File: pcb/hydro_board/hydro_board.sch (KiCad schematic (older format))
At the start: 1 part

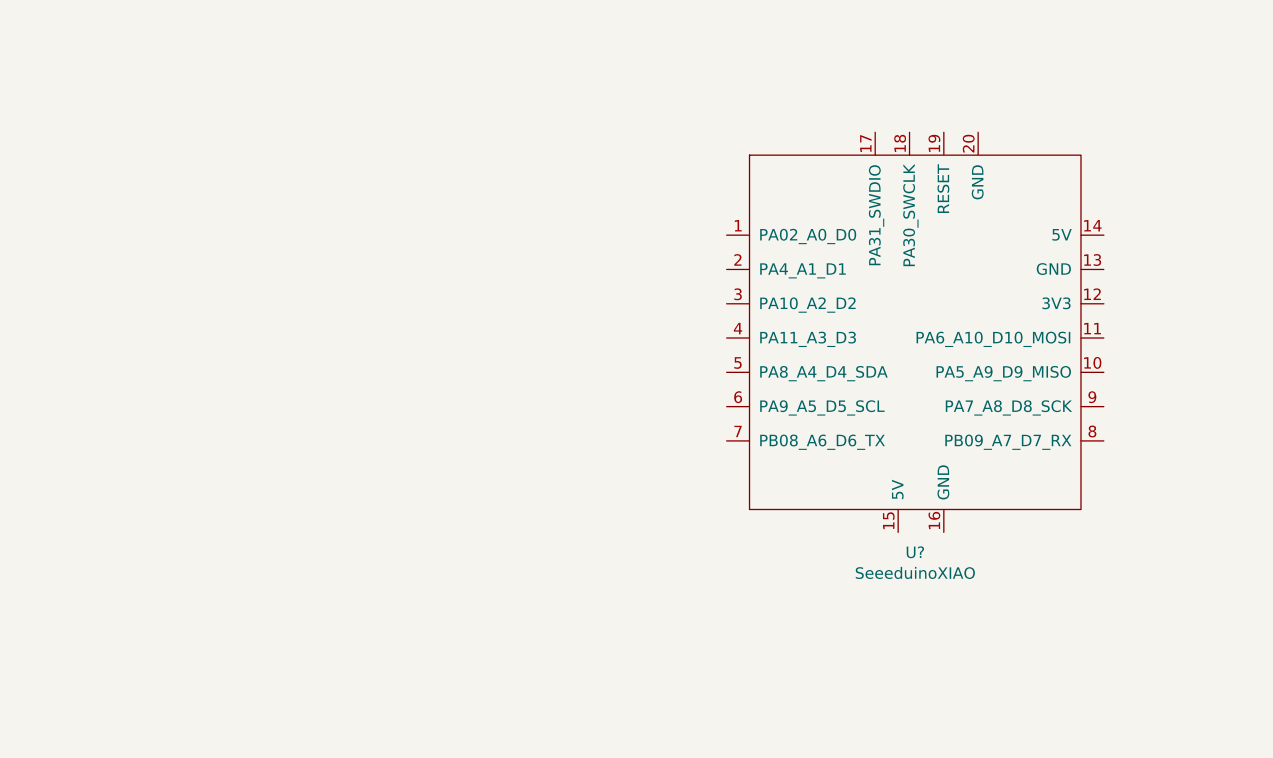
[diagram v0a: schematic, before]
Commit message: Updated schemetic
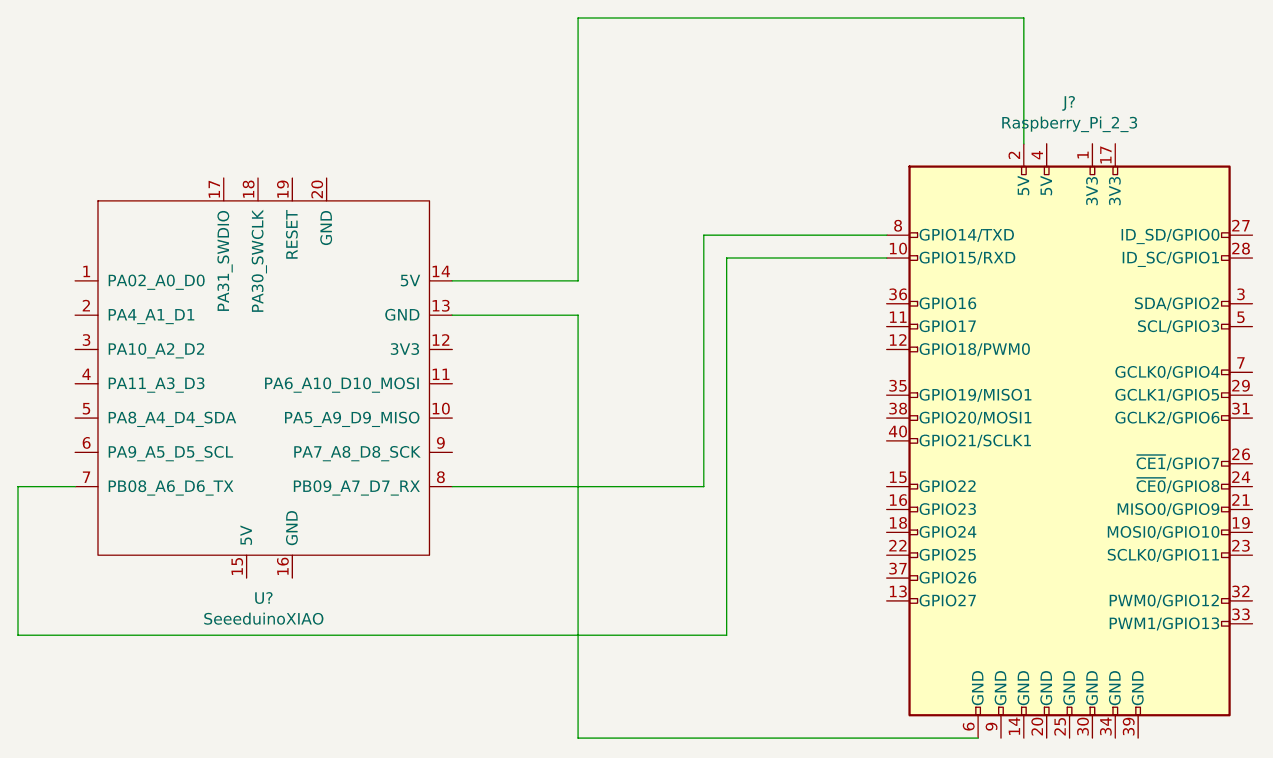
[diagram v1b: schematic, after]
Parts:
- added J?: Raspberry_Pi_2_3, symbol Connector:Raspberry_Pi_2_3
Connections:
- net at U?.13 (GND): now also J?.6 (GND)
- net at U?.14 (5V): now also J?.2 (5V)
- net at U?.7 (PB08_A6_D6_TX): now also J?.10 (GPIO15/RXD)
- net at U?.8 (PB09_A7_D7_RX): now also J?.8 (GPIO14/TXD)
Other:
- moved on the sheet: U?
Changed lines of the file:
@@
 L Seeeduino:SeeeduinoXIAO U?
 U 1 1 60A4ADD4
-P 8450 2650
-F 0 "U?" H 8425 1711 50  0000 C CNN
-F 1 "SeeeduinoXIAO" H 8425 1620 50  0000 C CNN
-F 2 "" H 8100 2850 50  0001 C CNN
-F 3 "" H 8100 2850 50  0001 C CNN
-	1    8450 2650
+P 5600 2850
+F 0 "U?" H 5575 1911 50  0000 C CNN
+F 1 "SeeeduinoXIAO" H 5575 1820 50  0000 C CNN
+F 2 "" H 5250 3050 50  0001 C CNN
+F 3 "" H 5250 3050 50  0001 C CNN
+	1    5600 2850
 	1    0    0    -1
 $EndComp
+$Comp
+L Connector:Raspberry_Pi_2_3 J?
+U 1 1 60ABEAF1
+P 9100 3100
+F 0 "J?" H 9100 4581 50  0000 C CNN
+F 1 "Raspberry_Pi_2_3" H 9100 4490 50  0000 C CNN
+F 2 "" H 9100 3100 50  0001 C CNN
+F 3 "https://www.raspberrypi.org/documentation/hardware/raspberrypi/schematics/rpi_SCH_3bplus_1p0_reduced.pdf" H 9100 3100 50  0001 C CNN
+	1    9100 3100
+	1    0    0    -1
+$EndComp
+Wire Wire Line
+	8900 1800 8900 1250
+Wire Wire Line
+	8900 1250 6950 1250
+Wire Wire Line
+	6950 1250 6950 2400
+Wire Wire Line
+	6950 2400 6400 2400
+Wire Wire Line
+	6950 4400 6950 2550
+Wire Wire Line
+	6950 2550 6400 2550
+Wire Wire Line
+	6950 4400 8700 4400
+Wire Wire Line
+	8300 2200 7500 2200
+Wire Wire Line
+	7500 2200 7500 3300
+Wire Wire Line
+	7500 3300 6400 3300
+Wire Wire Line
+	8300 2300 7600 2300
+Wire Wire Line
+	7600 2300 7600 3950
+Wire Wire Line
+	7600 3950 4500 3950
+Wire Wire Line
+	4500 3950 4500 3300
+Wire Wire Line
+	4500 3300 4750 3300
 $EndSCHEMATC
